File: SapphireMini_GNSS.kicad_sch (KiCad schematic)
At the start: 6 parts, among them J401 Conn_01x01_Male, U402 SAM-M8Q-0-10

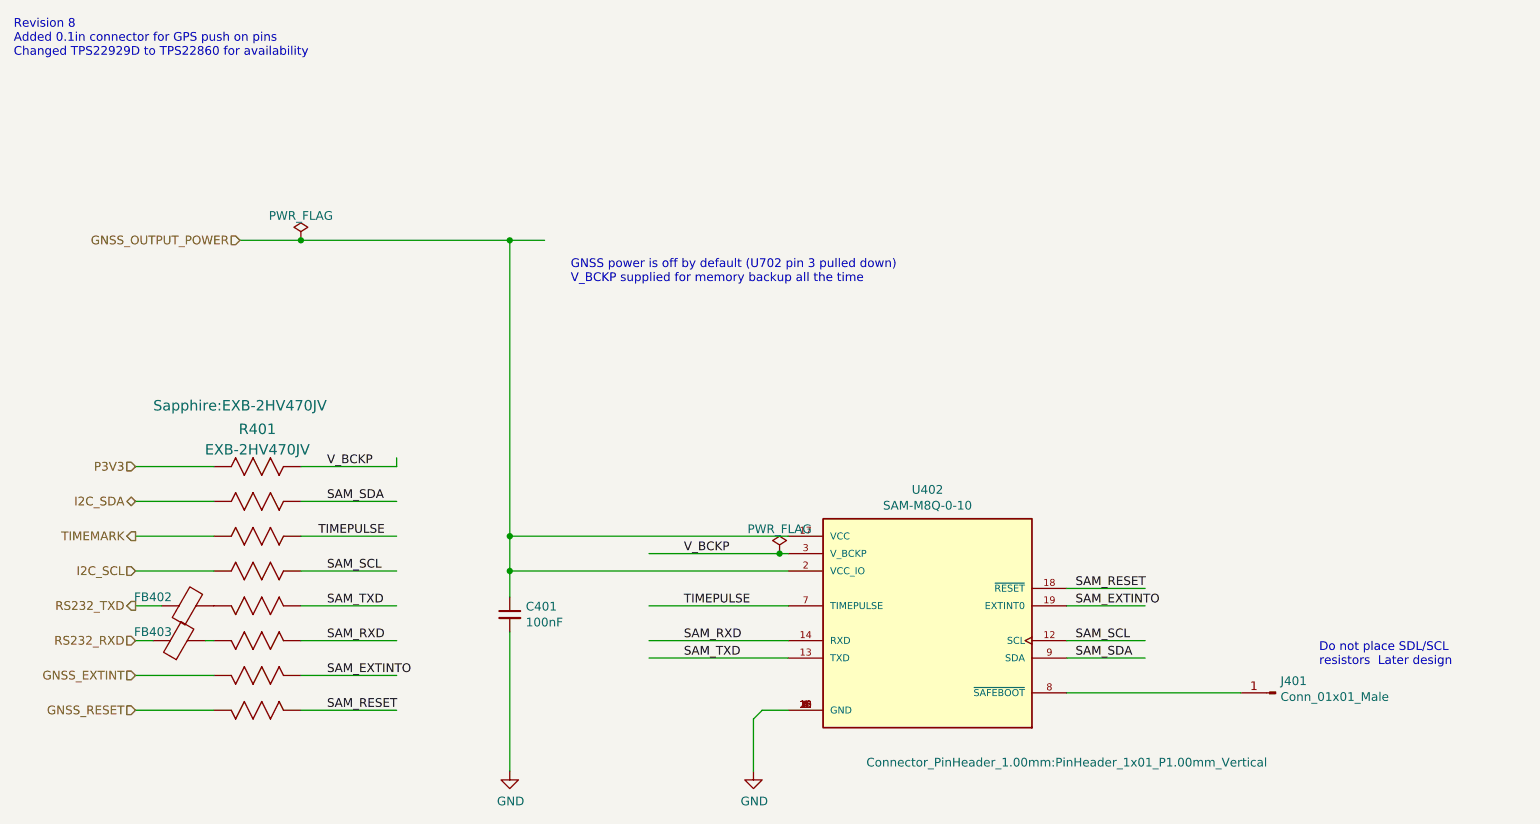
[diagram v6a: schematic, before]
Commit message: Updating for parts avail
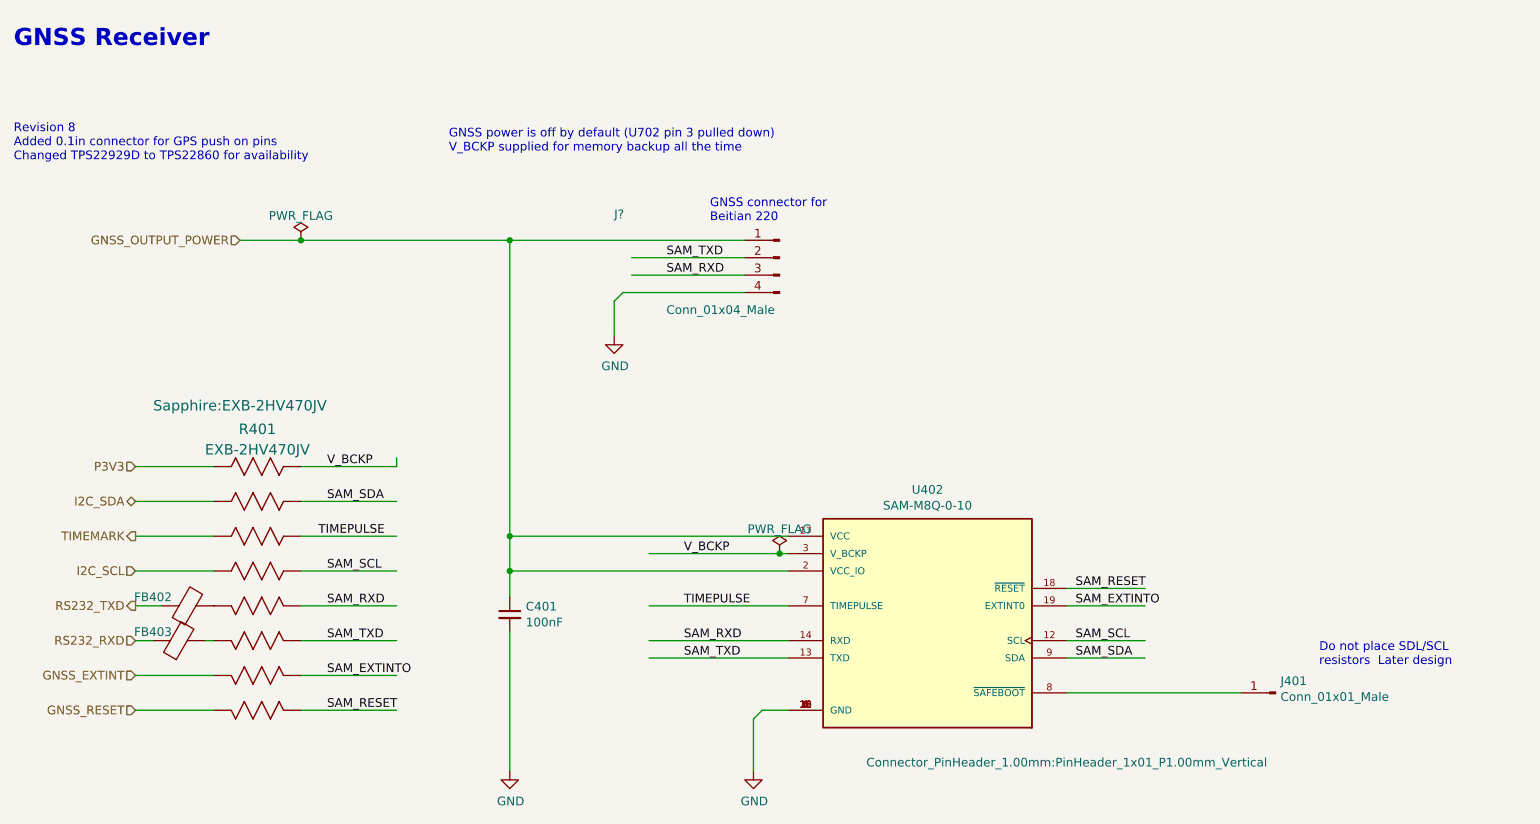
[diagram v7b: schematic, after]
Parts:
- added J?: Conn_01x04_Male, Connector_JST:JST_SH_SM04B-SRSS-TB_1x04-1MP_P1.00mm_Horizontal, symbol Connector:Conn_01x04_Male
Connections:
- net GND: now also J?.4 (Pin_4)
- net GNSS_OUTPUT_POWER: now also J?.1 (Pin_1)
- net SAM_RXD: now also R401.12, J?.3 (Pin_3); no longer R401.11
- net SAM_TXD: now also R401.11, J?.2 (Pin_2); no longer R401.12
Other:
- note added: "GNSS Receiver"
- note added: "GNSS connector for Beitian 220"
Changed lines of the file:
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@@
   (title_block
     (title "Sapphire Mini M2")
-    (date "2022-09-26")
+    (date "2022-10-04")
     (rev "1")
     (company "Southern Methodist Univ")
     (comment 1 "Chris Hayward")
+    (comment 2 "Markup copy w/ errors!")
   )
   (junction (at 64.77 46.99) (diameter 0) (color 0 0 0 0)
@@
     (stroke (width 0) (type default) (color 0 0 0 0))
   )
+  (wire (pts (xy 110.49 55.88) (xy 111.76 54.61))
+    (stroke (width 0) (type default) (color 0 0 0 0))
+  )
+  (wire (pts (xy 129.54 49.53) (xy 113.03 49.53))
+    (stroke (width 0) (type default) (color 0 0 0 0))
+  )
   (wire (pts (xy 64.77 80.01) (xy 78.74 80.01))
     (stroke (width 0) (type default) (color 0 0 0 0))
@@
     (stroke (width 0) (type default) (color 0 0 0 0))
   )
+  (wire (pts (xy 110.49 60.96) (xy 110.49 55.88))
+    (stroke (width 0) (type default) (color 0 0 0 0))
+  )
   (wire (pts (xy 40.64 100.33) (xy 44.45 100.33))
     (stroke (width 0) (type default) (color 0 0 0 0))
@@
     (stroke (width 0) (type default) (color 0 0 0 0))
   )
+  (wire (pts (xy 129.54 52.07) (xy 113.03 52.07))
+    (stroke (width 0) (type default) (color 0 0 0 0))
+  )
   (wire (pts (xy 64.77 90.17) (xy 78.74 90.17))
     (stroke (width 0) (type default) (color 0 0 0 0))
@@
     (stroke (width 0) (type default) (color 0 0 0 0))
   )
-  (wire (pts (xy 100.33 46.99) (xy 95.25 46.99))
+  (wire (pts (xy 95.25 46.99) (xy 129.54 46.99))
     (stroke (width 0) (type default) (color 0 0 0 0))
   )
@@
     (stroke (width 0) (type default) (color 0 0 0 0))
   )
+  (wire (pts (xy 111.76 54.61) (xy 129.54 54.61))
+    (stroke (width 0) (type default) (color 0 0 0 0))
+  )
   (wire (pts (xy 176.53 107.95) (xy 187.96 107.95))
     (stroke (width 0) (type default) (color 0 0 0 0))
   )
   (text "Revision 8\nAdded 0.1in connector for GPS push on pins\nChanged TPS22929D to TPS22860 for availability"
-    (at 22.86 20.32 0)
+    (at 22.86 35.56 0)
     (effects (font (size 1.27 1.27)) (justify left bottom))
   )
   (text "GNSS power is off by default (U702 pin 3 pulled down)\nV_BCKP supplied for memory backup all the time"
-    (at 104.14 53.34 0)
+    (at 86.36 34.29 0)
     (effects (font (size 1.27 1.27)) (justify left bottom))
   )
@@
     (effects (font (size 1.27 1.27)) (justify left bottom))
   )
+  (text "GNSS connector for\nBeitian 220\n" (at 124.46 44.45 0)
+    (effects (font (size 1.27 1.27)) (justify left bottom))
+  )
+  (text "GNSS Receiver" (at 22.86 19.05 0)
+    (effects (font (size 2.5 2.5) (thickness 0.5) bold) (justify left bottom))
+  )
   (label "SAM_RXD" (at 120.65 105.41 0)
     (effects (font (size 1.27 1.27)) (justify left bottom))
   )
+  (label "SAM_TXD" (at 118.11 49.53 0)
+    (effects (font (size 1.27 1.27)) (justify left bottom))
+  )
   (label "V_BCKP" (at 68.58 80.01 0)
     (effects (font (size 1.27 1.27)) (justify left bottom))
   )
+  (label "SAM_RXD" (at 118.11 52.07 0)
+    (effects (font (size 1.27 1.27)) (justify left bottom))
+  )
   (label "SAM_SDA" (at 68.58 85.09 0)
     (effects (font (size 1.27 1.27)) (justify left bottom))
   )
-  (label "SAM_RXD" (at 68.58 105.41 0)
+  (label "SAM_RXD" (at 68.58 100.33 0)
     (effects (font (size 1.27 1.27)) (justify left bottom))
   )
@@
     (effects (font (size 1.27 1.27)) (justify left bottom))
   )
-  (label "SAM_TXD" (at 68.58 100.33 0)
+  (label "SAM_TXD" (at 68.58 105.41 0)
     (effects (font (size 1.27 1.27)) (justify left bottom))
   )
@@
     (pin "2")
   )
+  (symbol (lib_id "Connector:Conn_01x04_Male") (at 134.62 49.53 0) (mirror y) (unit 1)
+    (in_bom yes) (on_board yes)
+    (property "Reference" "J?" (id 0) (at 110.49 43.18 0)
+      (effects (font (size 1.27 1.27)) (justify right))
+    )
+    (property "Value" "Conn_01x04_Male" (id 1) (at 118.11 57.15 0)
+      (effects (font (size 1.27 1.27)) (justify right))
+    )
+    (property "Footprint" "Connector_JST:JST_SH_SM04B-SRSS-TB_1x04-1MP_P1.00mm_Horizontal" (id 2) (at 134.62 49.53 0)
+      (effects (font (size 1.27 1.27)) hide)
+    )
+    (property "Datasheet" "~" (id 3) (at 134.62 49.53 0)
+      (effects (font (size 1.27 1.27)) hide)
+    )
+    (property "DPN" "455-1804-1-ND" (id 4) (at 134.62 49.53 0)
+      (effects (font (size 1.27 1.27)) hide)
+    )
+    (property "MPN" "SM04B-SRSS-TB(LF)(SN)" (id 5) (at 134.62 49.53 0)
+      (effects (font (size 1.27 1.27)) hide)
+    )
+    (property "Manufacturer" "JST" (id 6) (at 134.62 49.53 0)
+      (effects (font (size 1.27 1.27)) hide)
+    )
+    (property "Populate" "1" (id 7) (at 134.62 49.53 0)
+      (effects (font (size 1.27 1.27)) hide)
+    )
+    (property "Description" "Connector Header Surface Mount, Right Angle 4 position 0.039\" (1.00mm)" (id 8) (at 134.62 49.53 0)
+      (effects (font (size 1.27 1.27)) hide)
+    )
+    (property "Digi-Key_PN" "455-1804-1-ND" (id 9) (at 134.62 49.53 0)
+      (effects (font (size 1.27 1.27)) hide)
+    )
+    (property "OnHand" "221" (id 10) (at 134.62 49.53 0)
+      (effects (font (size 1.27 1.27)) hide)
+    )
+    (property "Status" "" (id 11) (at 134.62 49.53 0)
+      (effects (font (size 1.27 1.27)) hide)
+    )
+    (property "Distributor" "Digikey" (id 12) (at 134.62 49.53 0)
+      (effects (font (size 1.27 1.27)) hide)
+    )
+    (pin "1")
+    (pin "2")
+    (pin "3")
+    (pin "4")
+  )
   (symbol (lib_id "power:GND") (at 95.25 124.46 0) (unit 1)
     (in_bom yes) (on_board yes)
@@
       (effects (font (size 1.27 1.27)) hide)
     )
+    (pin "1")
+  )
+  (symbol (lib_id "power:GND") (at 110.49 60.96 0) (unit 1)
+    (in_bom yes) (on_board yes)
+    (property "Reference" "#PWR?" (id 0) (at 110.49 67.31 0)
+      (effects (font (size 1.27 1.27)) hide)
+    )
+    (property "Value" "GND" (id 1) (at 110.617 65.3542 0))
+    (property "Footprint" "" (id 2) (at 110.49 60.96 0)
+      (effects (font (size 1.27 1.27)) hide)
+    )
+    (property "Datasheet" "" (id 3) (at 110.49 60.96 0)
+      (effects (font (size 1.27 1.27)) hide)
+    )

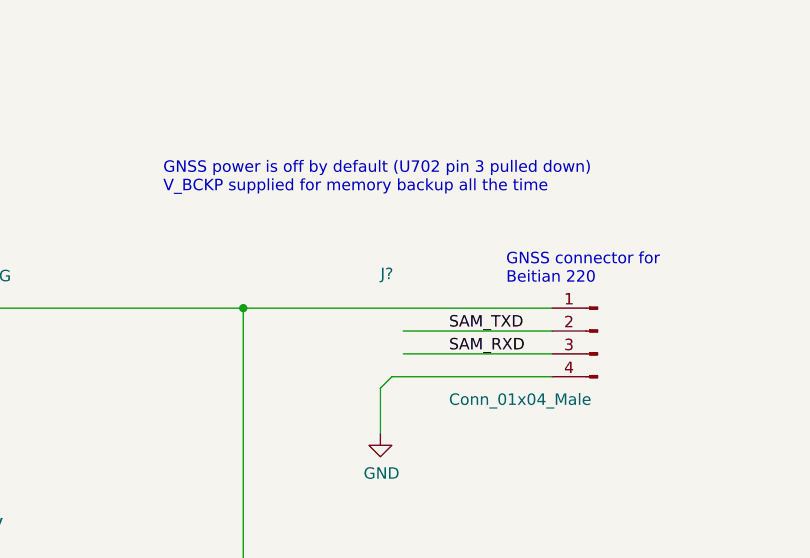
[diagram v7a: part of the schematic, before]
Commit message: Skematic updated for power and 1PSI sensor
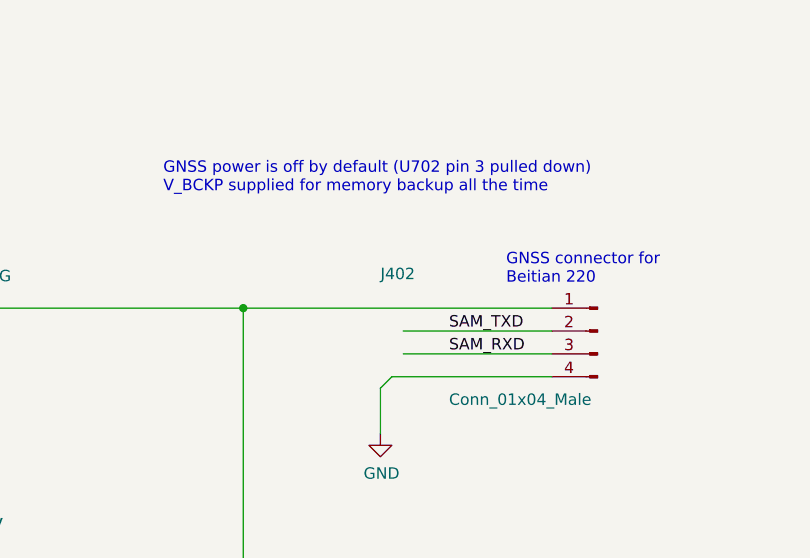
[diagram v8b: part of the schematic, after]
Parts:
- gave numbers to parts that had none: 1
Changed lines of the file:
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@@
   (symbol (lib_id "Connector:Conn_01x04_Male") (at 134.62 49.53 0) (mirror y) (unit 1)
     (in_bom yes) (on_board yes)
-    (property "Reference" "J?" (id 0) (at 110.49 43.18 0)
+    (property "Reference" "J402" (id 0) (at 110.49 43.18 0)
       (effects (font (size 1.27 1.27)) (justify right))
     )
@@
   (symbol (lib_id "power:GND") (at 110.49 60.96 0) (unit 1)
     (in_bom yes) (on_board yes)
-    (property "Reference" "#PWR?" (id 0) (at 110.49 67.31 0)
+    (property "Reference" "#PWR0101" (id 0) (at 110.49 67.31 0)
       (effects (font (size 1.27 1.27)) hide)
     )
